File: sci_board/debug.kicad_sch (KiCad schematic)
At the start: 13 parts, among them J10 Conn_01x03_Pin, J11 Conn_01x03_Pin, J12 Conn_01x03_Pin

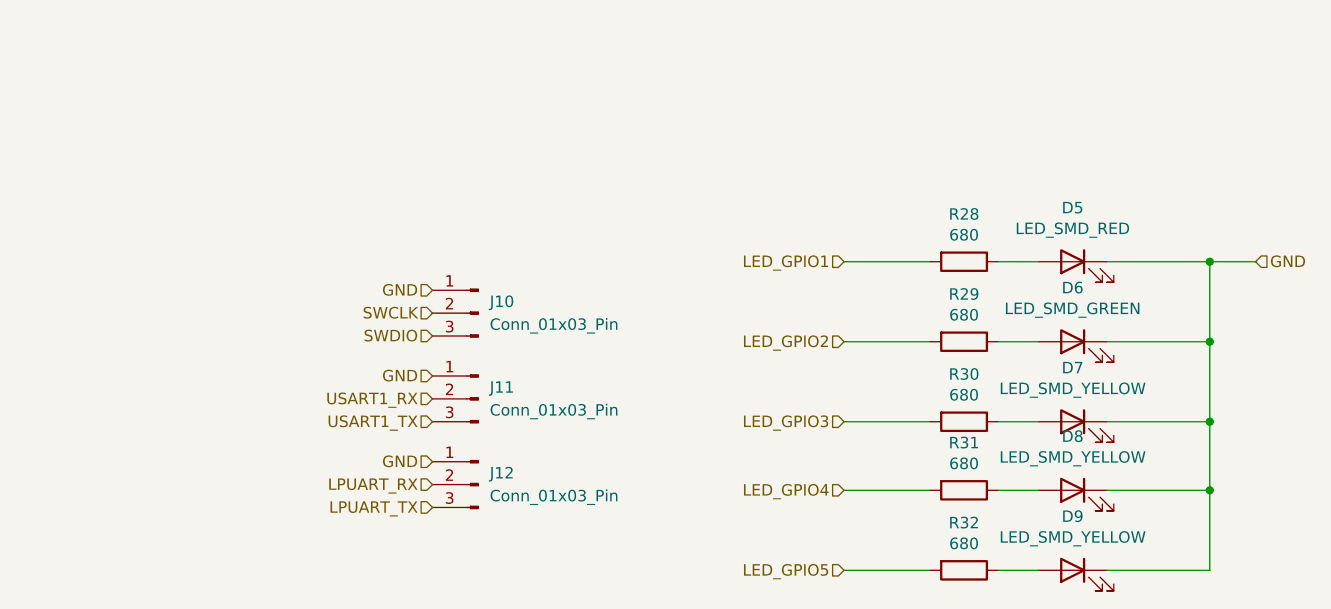
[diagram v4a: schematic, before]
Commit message: push PC104 bus reorder (no more 5V, 20 lines of 3V3 and 4 switched batt) to system components
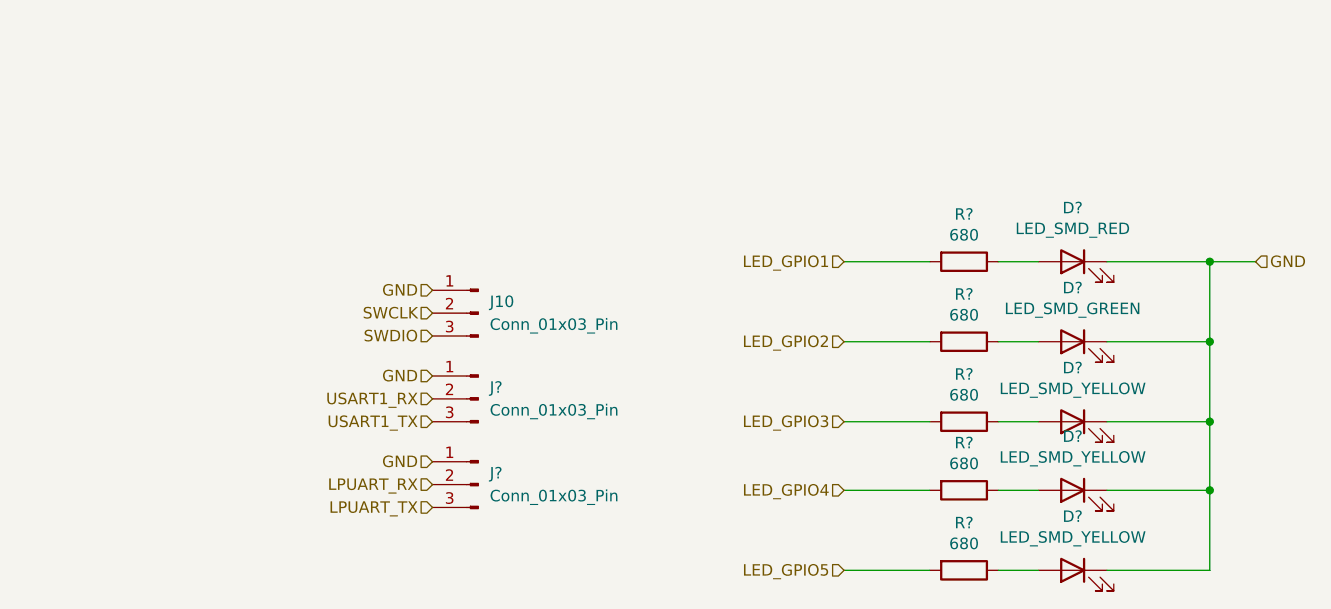
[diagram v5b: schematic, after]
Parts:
- renumbered D8 to D?, D9 to D?, D5 to D?, D6 to D?, D7 to D?, J12 to J?, J11 to J?, R31 to R?, R32 to R?, R29 to R?, R28 to R?, R30 to R?
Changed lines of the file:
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@@
 		(on_board yes)
 		(dnp no)
-		(property "Reference" "D8"
+		(property "Reference" "D?"
 			(at 133.35 60.071 0)
 			(effects
@@
 		)
 		(instances
-			(project "sci_board"
-				(path "/a863a5ec-a5d4-4f54-be53-e8c01d5e3ac4/53f12969-e593-459a-9671-cc23a5a9aea0/f4ff56ce-2fa2-4b99-a709-c113709260c1/730bd731-7be7-49ed-966d-7ccd975f4386"
-					(reference "D8")
+			(project "openlst-hw"
+				(path "/a863a5ec-a5d4-4f54-be53-e8c01d5e3ac4/53f12969-e593-459a-9671-cc23a5a9aea0/f4ff56ce-2fa2-4b99-a709-c113709260c1/730bd731-7be7-49ed-966d-7ccd975f4386"
+					(reference "D?")
 					(unit 1)
 				)
@@
 		(on_board yes)
 		(dnp no)
-		(property "Reference" "R31"
+		(property "Reference" "R?"
 			(at 121.285 60.7822 90)
 			(effects
@@
 		)
 		(instances
-			(project "sci_board"
-				(path "/a863a5ec-a5d4-4f54-be53-e8c01d5e3ac4/53f12969-e593-459a-9671-cc23a5a9aea0/f4ff56ce-2fa2-4b99-a709-c113709260c1/730bd731-7be7-49ed-966d-7ccd975f4386"
-					(reference "R31")
+			(project "openlst-hw"
+				(path "/a863a5ec-a5d4-4f54-be53-e8c01d5e3ac4/53f12969-e593-459a-9671-cc23a5a9aea0/f4ff56ce-2fa2-4b99-a709-c113709260c1/730bd731-7be7-49ed-966d-7ccd975f4386"
+					(reference "R?")
 					(unit 1)
 				)
@@
 		(on_board yes)
 		(dnp no)
-		(property "Reference" "R32"
+		(property "Reference" "R?"
 			(at 121.285 69.6722 90)
 			(effects
@@
 		)
 		(instances
-			(project "sci_board"
-				(path "/a863a5ec-a5d4-4f54-be53-e8c01d5e3ac4/53f12969-e593-459a-9671-cc23a5a9aea0/f4ff56ce-2fa2-4b99-a709-c113709260c1/730bd731-7be7-49ed-966d-7ccd975f4386"
-					(reference "R32")
+			(project "openlst-hw"
+				(path "/a863a5ec-a5d4-4f54-be53-e8c01d5e3ac4/53f12969-e593-459a-9671-cc23a5a9aea0/f4ff56ce-2fa2-4b99-a709-c113709260c1/730bd731-7be7-49ed-966d-7ccd975f4386"
+					(reference "R?")
 					(unit 1)
 				)
@@
 		(on_board yes)
 		(dnp no)
-		(property "Reference" "D9"
+		(property "Reference" "D?"
 			(at 133.35 68.961 0)
 			(effects
@@
 		)
 		(instances
-			(project "sci_board"
-				(path "/a863a5ec-a5d4-4f54-be53-e8c01d5e3ac4/53f12969-e593-459a-9671-cc23a5a9aea0/f4ff56ce-2fa2-4b99-a709-c113709260c1/730bd731-7be7-49ed-966d-7ccd975f4386"
-					(reference "D9")
+			(project "openlst-hw"
+				(path "/a863a5ec-a5d4-4f54-be53-e8c01d5e3ac4/53f12969-e593-459a-9671-cc23a5a9aea0/f4ff56ce-2fa2-4b99-a709-c113709260c1/730bd731-7be7-49ed-966d-7ccd975f4386"
+					(reference "D?")
 					(unit 1)
 				)
@@
 		(on_board yes)
 		(dnp no)
-		(property "Reference" "R29"
+		(property "Reference" "R?"
 			(at 121.285 44.2722 90)
 			(effects
@@
 		)
 		(instances
-			(project "sci_board"
-				(path "/a863a5ec-a5d4-4f54-be53-e8c01d5e3ac4/53f12969-e593-459a-9671-cc23a5a9aea0/f4ff56ce-2fa2-4b99-a709-c113709260c1/730bd731-7be7-49ed-966d-7ccd975f4386"
-					(reference "R29")
+			(project "openlst-hw"
+				(path "/a863a5ec-a5d4-4f54-be53-e8c01d5e3ac4/53f12969-e593-459a-9671-cc23a5a9aea0/f4ff56ce-2fa2-4b99-a709-c113709260c1/730bd731-7be7-49ed-966d-7ccd975f4386"
+					(reference "R?")
 					(unit 1)
 				)
@@
 		(on_board yes)
 		(dnp no)
-		(property "Reference" "D5"
+		(property "Reference" "D?"
 			(at 133.35 34.671 0)
 			(effects
@@
 		)
 		(instances
-			(project "sci_board"
-				(path "/a863a5ec-a5d4-4f54-be53-e8c01d5e3ac4/53f12969-e593-459a-9671-cc23a5a9aea0/f4ff56ce-2fa2-4b99-a709-c113709260c1/730bd731-7be7-49ed-966d-7ccd975f4386"
-					(reference "D5")
+			(project "openlst-hw"
+				(path "/a863a5ec-a5d4-4f54-be53-e8c01d5e3ac4/53f12969-e593-459a-9671-cc23a5a9aea0/f4ff56ce-2fa2-4b99-a709-c113709260c1/730bd731-7be7-49ed-966d-7ccd975f4386"
+					(reference "D?")
 					(unit 1)
 				)
@@
 		(dnp no)
 		(fields_autoplaced yes)
-		(property "Reference" "J12"
+		(property "Reference" "J?"
 			(at 68.58 64.1349 0)
 			(effects
@@
 		)
 		(instances
-			(project "sci_board"
-				(path "/a863a5ec-a5d4-4f54-be53-e8c01d5e3ac4/53f12969-e593-459a-9671-cc23a5a9aea0/f4ff56ce-2fa2-4b99-a709-c113709260c1/730bd731-7be7-49ed-966d-7ccd975f4386"
-					(reference "J12")
+			(project "openlst-hw"
+				(path "/a863a5ec-a5d4-4f54-be53-e8c01d5e3ac4/53f12969-e593-459a-9671-cc23a5a9aea0/f4ff56ce-2fa2-4b99-a709-c113709260c1/730bd731-7be7-49ed-966d-7ccd975f4386"
+					(reference "J?")
 					(unit 1)
 				)
@@
 		(on_board yes)
 		(dnp no)
-		(property "Reference" "R28"
+		(property "Reference" "R?"
 			(at 121.285 35.3822 90)
 			(effects
@@
 		)
 		(instances
-			(project "sci_board"
-				(path "/a863a5ec-a5d4-4f54-be53-e8c01d5e3ac4/53f12969-e593-459a-9671-cc23a5a9aea0/f4ff56ce-2fa2-4b99-a709-c113709260c1/730bd731-7be7-49ed-966d-7ccd975f4386"
-					(reference "R28")
+			(project "openlst-hw"
+				(path "/a863a5ec-a5d4-4f54-be53-e8c01d5e3ac4/53f12969-e593-459a-9671-cc23a5a9aea0/f4ff56ce-2fa2-4b99-a709-c113709260c1/730bd731-7be7-49ed-966d-7ccd975f4386"
+					(reference "R?")
 					(unit 1)
 				)
@@
 		(dnp no)
 		(fields_autoplaced yes)
-		(property "Reference" "J11"
+		(property "Reference" "J?"
 			(at 68.58 54.6099 0)
 			(effects
@@
 		)
 		(instances
-			(project "sci_board"
-				(path "/a863a5ec-a5d4-4f54-be53-e8c01d5e3ac4/53f12969-e593-459a-9671-cc23a5a9aea0/f4ff56ce-2fa2-4b99-a709-c113709260c1/730bd731-7be7-49ed-966d-7ccd975f4386"
-					(reference "J11")
+			(project "openlst-hw"
+				(path "/a863a5ec-a5d4-4f54-be53-e8c01d5e3ac4/53f12969-e593-459a-9671-cc23a5a9aea0/f4ff56ce-2fa2-4b99-a709-c113709260c1/730bd731-7be7-49ed-966d-7ccd975f4386"
+					(reference "J?")
 					(unit 1)
 				)
@@
 		(on_board yes)
 		(dnp no)
-		(property "Reference" "D6"
+		(property "Reference" "D?"
 			(at 133.35 43.561 0)
 			(effects
@@
 		)
 		(instances
-			(project "sci_board"
-				(path "/a863a5ec-a5d4-4f54-be53-e8c01d5e3ac4/53f12969-e593-459a-9671-cc23a5a9aea0/f4ff56ce-2fa2-4b99-a709-c113709260c1/730bd731-7be7-49ed-966d-7ccd975f4386"
-					(reference "D6")
+			(project "openlst-hw"
+				(path "/a863a5ec-a5d4-4f54-be53-e8c01d5e3ac4/53f12969-e593-459a-9671-cc23a5a9aea0/f4ff56ce-2fa2-4b99-a709-c113709260c1/730bd731-7be7-49ed-966d-7ccd975f4386"
+					(reference "D?")
 					(unit 1)
 				)
@@
 		(on_board yes)
 		(dnp no)
-		(property "Reference" "D7"
+		(property "Reference" "D?"
 			(at 133.35 52.451 0)
 			(effects
@@
 		)
 		(instances
-			(project "sci_board"
-				(path "/a863a5ec-a5d4-4f54-be53-e8c01d5e3ac4/53f12969-e593-459a-9671-cc23a5a9aea0/f4ff56ce-2fa2-4b99-a709-c113709260c1/730bd731-7be7-49ed-966d-7ccd975f4386"
-					(reference "D7")
+			(project "openlst-hw"
+				(path "/a863a5ec-a5d4-4f54-be53-e8c01d5e3ac4/53f12969-e593-459a-9671-cc23a5a9aea0/f4ff56ce-2fa2-4b99-a709-c113709260c1/730bd731-7be7-49ed-966d-7ccd975f4386"
+					(reference "D?")
 					(unit 1)
 				)
@@
 		(on_board yes)
 		(dnp no)
-		(property "Reference" "R30"
+		(property "Reference" "R?"
 			(at 121.285 53.1622 90)
 			(effects
@@
 		)
 		(instances
-			(project "sci_board"
-				(path "/a863a5ec-a5d4-4f54-be53-e8c01d5e3ac4/53f12969-e593-459a-9671-cc23a5a9aea0/f4ff56ce-2fa2-4b99-a709-c113709260c1/730bd731-7be7-49ed-966d-7ccd975f4386"
-					(reference "R30")
-					(unit 1)
-				)
+			(project "openlst-hw"
+				(path "/a863a5ec-a5d4-4f54-be53-e8c01d5e3ac4/53f12969-e593-459a-9671-cc23a5a9aea0/f4ff56ce-2fa2-4b99-a709-c113709260c1/730bd731-7be7-49ed-966d-7ccd975f4386"
+					(reference "R?")
+					(unit 1)
+				)

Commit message: openlst board
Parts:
- gave numbers to parts that had none: 12
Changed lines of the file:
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@@
 		(on_board yes)
 		(dnp no)
-		(property "Reference" "D?"
+		(property "Reference" "D8"
 			(at 133.35 60.071 0)
 			(effects
@@
 			(project "openlst-hw"
 				(path "/a863a5ec-a5d4-4f54-be53-e8c01d5e3ac4/53f12969-e593-459a-9671-cc23a5a9aea0/f4ff56ce-2fa2-4b99-a709-c113709260c1/730bd731-7be7-49ed-966d-7ccd975f4386"
-					(reference "D?")
+					(reference "D8")
 					(unit 1)
 				)
@@
 		(on_board yes)
 		(dnp no)
-		(property "Reference" "R?"
+		(property "Reference" "R31"
 			(at 121.285 60.7822 90)
 			(effects
@@
 			(project "openlst-hw"
 				(path "/a863a5ec-a5d4-4f54-be53-e8c01d5e3ac4/53f12969-e593-459a-9671-cc23a5a9aea0/f4ff56ce-2fa2-4b99-a709-c113709260c1/730bd731-7be7-49ed-966d-7ccd975f4386"
-					(reference "R?")
+					(reference "R31")
 					(unit 1)
 				)
@@
 		(on_board yes)
 		(dnp no)
-		(property "Reference" "R?"
+		(property "Reference" "R32"
 			(at 121.285 69.6722 90)
 			(effects
@@
 			(project "openlst-hw"
 				(path "/a863a5ec-a5d4-4f54-be53-e8c01d5e3ac4/53f12969-e593-459a-9671-cc23a5a9aea0/f4ff56ce-2fa2-4b99-a709-c113709260c1/730bd731-7be7-49ed-966d-7ccd975f4386"
-					(reference "R?")
+					(reference "R32")
 					(unit 1)
 				)
@@
 		(on_board yes)
 		(dnp no)
-		(property "Reference" "D?"
+		(property "Reference" "D9"
 			(at 133.35 68.961 0)
 			(effects
@@
 			(project "openlst-hw"
 				(path "/a863a5ec-a5d4-4f54-be53-e8c01d5e3ac4/53f12969-e593-459a-9671-cc23a5a9aea0/f4ff56ce-2fa2-4b99-a709-c113709260c1/730bd731-7be7-49ed-966d-7ccd975f4386"
-					(reference "D?")
+					(reference "D9")
 					(unit 1)
 				)
@@
 		(on_board yes)
 		(dnp no)
-		(property "Reference" "R?"
+		(property "Reference" "R29"
 			(at 121.285 44.2722 90)
 			(effects
@@
 			(project "openlst-hw"
 				(path "/a863a5ec-a5d4-4f54-be53-e8c01d5e3ac4/53f12969-e593-459a-9671-cc23a5a9aea0/f4ff56ce-2fa2-4b99-a709-c113709260c1/730bd731-7be7-49ed-966d-7ccd975f4386"
-					(reference "R?")
+					(reference "R29")
 					(unit 1)
 				)
@@
 		(on_board yes)
 		(dnp no)
-		(property "Reference" "D?"
+		(property "Reference" "D5"
 			(at 133.35 34.671 0)
 			(effects
@@
 			(project "openlst-hw"
 				(path "/a863a5ec-a5d4-4f54-be53-e8c01d5e3ac4/53f12969-e593-459a-9671-cc23a5a9aea0/f4ff56ce-2fa2-4b99-a709-c113709260c1/730bd731-7be7-49ed-966d-7ccd975f4386"
-					(reference "D?")
+					(reference "D5")
 					(unit 1)
 				)
@@
 		(dnp no)
 		(fields_autoplaced yes)
-		(property "Reference" "J?"
+		(property "Reference" "J12"
 			(at 68.58 64.1349 0)
 			(effects
@@
 			(project "openlst-hw"
 				(path "/a863a5ec-a5d4-4f54-be53-e8c01d5e3ac4/53f12969-e593-459a-9671-cc23a5a9aea0/f4ff56ce-2fa2-4b99-a709-c113709260c1/730bd731-7be7-49ed-966d-7ccd975f4386"
-					(reference "J?")
+					(reference "J12")
 					(unit 1)
 				)
@@
 		(on_board yes)
 		(dnp no)
-		(property "Reference" "R?"
+		(property "Reference" "R28"
 			(at 121.285 35.3822 90)
 			(effects
@@
 			(project "openlst-hw"
 				(path "/a863a5ec-a5d4-4f54-be53-e8c01d5e3ac4/53f12969-e593-459a-9671-cc23a5a9aea0/f4ff56ce-2fa2-4b99-a709-c113709260c1/730bd731-7be7-49ed-966d-7ccd975f4386"
-					(reference "R?")
+					(reference "R28")
 					(unit 1)
 				)
@@
 		(dnp no)
 		(fields_autoplaced yes)
-		(property "Reference" "J?"
+		(property "Reference" "J11"
 			(at 68.58 54.6099 0)
 			(effects
@@
 			(project "openlst-hw"
 				(path "/a863a5ec-a5d4-4f54-be53-e8c01d5e3ac4/53f12969-e593-459a-9671-cc23a5a9aea0/f4ff56ce-2fa2-4b99-a709-c113709260c1/730bd731-7be7-49ed-966d-7ccd975f4386"
-					(reference "J?")
+					(reference "J11")
 					(unit 1)
 				)
@@
 		(on_board yes)
 		(dnp no)
-		(property "Reference" "D?"
+		(property "Reference" "D6"
 			(at 133.35 43.561 0)
 			(effects
@@
 			(project "openlst-hw"
 				(path "/a863a5ec-a5d4-4f54-be53-e8c01d5e3ac4/53f12969-e593-459a-9671-cc23a5a9aea0/f4ff56ce-2fa2-4b99-a709-c113709260c1/730bd731-7be7-49ed-966d-7ccd975f4386"
-					(reference "D?")
+					(reference "D6")
 					(unit 1)
 				)
@@
 		(on_board yes)
 		(dnp no)
-		(property "Reference" "D?"
+		(property "Reference" "D7"
 			(at 133.35 52.451 0)
 			(effects
@@
 			(project "openlst-hw"
 				(path "/a863a5ec-a5d4-4f54-be53-e8c01d5e3ac4/53f12969-e593-459a-9671-cc23a5a9aea0/f4ff56ce-2fa2-4b99-a709-c113709260c1/730bd731-7be7-49ed-966d-7ccd975f4386"
-					(reference "D?")
+					(reference "D7")
 					(unit 1)
 				)
@@
 		(on_board yes)
 		(dnp no)
-		(property "Reference" "R?"
+		(property "Reference" "R30"
 			(at 121.285 53.1622 90)
 			(effects
@@
 			(project "openlst-hw"
 				(path "/a863a5ec-a5d4-4f54-be53-e8c01d5e3ac4/53f12969-e593-459a-9671-cc23a5a9aea0/f4ff56ce-2fa2-4b99-a709-c113709260c1/730bd731-7be7-49ed-966d-7ccd975f4386"
-					(reference "R?")
-					(unit 1)
-				)
+					(reference "R30")
+					(unit 1)
+				)

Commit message: SCI BOM updated
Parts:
- D5: Manufacturer (none) -> Lite-On; Mfr. # 150060RS75000 -> (none); Order https://www.digikey.com/product-detail/en/w%C3%BCrth-elektr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 -> (none); Part Number (none) -> LTST-C191KRKT; Voltage (none) -> 2
- D6: Manufacturer (none) -> Lite-On; Mfr. # 150060VS75000 -> (none); Order https://www.digikey.com/product-detail/en/w%C3%BCrth-elektr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 -> (none); Part Number (none) -> LTST-C191KGKT; Voltage (none) -> 2
- D7, D8, D9: Manufacturer (none) -> Lite-On; Mfr. # 150060YS75000 -> (none); Order https://www.digikey.com/product-detail/en/w%C3%BCrth-elektr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 -> (none); Part Number (none) -> LTST-C191KSKT; Voltage (none) -> 2
- J10, J11, J12: now not fitted
- R28, R29, R30, R31, R32: value 680 -> 1K; Manufacturer (none) -> YAGEO; Mfr. # CRCW0603330RJNEA -> (none); Note (none) -> LED; Order https://www.mouser.com/ProductDetail/Vishay-Dale/CRCW060333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 -> (none); Part Number (none) -> RC0402FR-071KL; Tolerance (none) -> 1

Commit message: RF board BOM
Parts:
- D5: value LED_SMD_RED -> RED
- D6: value LED_SMD_GREEN -> GREEN
- D7, D8, D9: value LED_SMD_YELLOW -> YELLOW
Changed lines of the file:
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@@
+			)
+		)
+		(property "Color" ""
+			(at 67.31 46.355 0)
+			(effects
+				(font
+					(size 1.27 1.27)
+				)
+				(hide yes)
 			)
 		)
@@
 			)
 		)
-		(property "Value" "LED_SMD_YELLOW"
+		(property "Value" "YELLOW"
 			(at 133.35 62.3824 0)
 			(effects
@@
 		)
 		(property "Note" ""
+			(at 133.35 66.04 0)
+			(effects
+				(font
+					(size 1.27 1.27)
+				)
+				(hide yes)
+			)
+		)
+		(property "Color" ""
 			(at 133.35 66.04 0)
 			(effects
@@
 			)
 		)
+		(property "Color" ""
+			(at 121.285 66.04 0)
+			(effects
+				(font
+					(size 1.27 1.27)
+				)
+				(hide yes)
+			)
+		)
 		(pin "1"
 		)
@@
 		)
 		(property "Tolerance" "1"
+			(at 121.285 74.93 0)
+			(effects
+				(font
+					(size 1.27 1.27)
+				)
+				(hide yes)
+			)
+		)
+		(property "Color" ""
 			(at 121.285 74.93 0)
 			(effects
@@
 			)
 		)
-		(property "Value" "LED_SMD_YELLOW"
+		(property "Value" "YELLOW"
 			(at 133.35 71.2724 0)
 			(effects
@@
 		)
 		(property "Note" ""
+			(at 133.35 74.93 0)
+			(effects
+				(font
+					(size 1.27 1.27)
+				)
+				(hide yes)
+			)
+		)
+		(property "Color" ""
 			(at 133.35 74.93 0)
 			(effects
@@
 		)
 		(property "Tolerance" "1"
+			(at 121.285 49.53 0)
+			(effects
+				(font
+					(size 1.27 1.27)
+				)
+				(hide yes)
+			)
+		)
+		(property "Color" ""
 			(at 121.285 49.53 0)
 			(effects
@@
 			)
 		)
-		(property "Value" "LED_SMD_RED"
+		(property "Value" "RED"
 			(at 133.35 36.9824 0)
 			(effects
@@
 		)
 		(property "Note" ""
+			(at 133.35 40.64 0)
+			(effects
+				(font
+					(size 1.27 1.27)
+				)
+				(hide yes)
+			)
+		)
+		(property "Color" ""
 			(at 133.35 40.64 0)
 			(effects
@@
 			)
 		)
+		(property "Color" ""
+			(at 67.31 65.405 0)
+			(effects
+				(font
+					(size 1.27 1.27)
+				)
+				(hide yes)
+			)
+		)
 		(pin "1"
 		)
@@
 		)
 		(property "Tolerance" "1"
+			(at 121.285 40.64 0)
+			(effects
+				(font
+					(size 1.27 1.27)
+				)
+				(hide yes)
+			)
+		)
+		(property "Color" ""
 			(at 121.285 40.64 0)
 			(effects
@@
 			)
 		)
+		(property "Color" ""
+			(at 67.31 55.88 0)
+			(effects
+				(font
+					(size 1.27 1.27)
+				)
+				(hide yes)
+			)
+		)
 		(pin "1"
 		)
@@
 			)
 		)
-		(property "Value" "LED_SMD_GREEN"
+		(property "Value" "GREEN"
 			(at 133.35 45.8724 0)
 			(effects
@@
 		)
 		(property "Note" ""
+			(at 133.35 49.53 0)
+			(effects
+				(font
+					(size 1.27 1.27)
+				)
+				(hide yes)
+			)
+		)
+		(property "Color" ""
 			(at 133.35 49.53 0)
 			(effects
@@
 			)
 		)
-		(property "Value" "LED_SMD_YELLOW"
+		(property "Value" "YELLOW"
 			(at 133.35 54.7624 0)
 			(effects
@@
 		)
 		(property "Note" ""
+			(at 133.35 58.42 0)
+			(effects
+				(font
+					(size 1.27 1.27)
+				)
+				(hide yes)
+			)
+		)
+		(property "Color" ""
 			(at 133.35 58.42 0)
 			(effects
@@
 			(at 121.285 58.42 0)
 			(effects
+				(font
+					(size 1.27 1.27)
+				)
+				(hide yes)
+			)
+		)
+		(property "Color" ""
+			(at 121.285 58.42 0)
+			(effects
